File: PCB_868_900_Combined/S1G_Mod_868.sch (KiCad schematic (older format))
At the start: 56 parts, among them Q1 DMG2307L-7, SW1 CUS-12TB, T1 0732511150, U1 AP7361-33FGE-7, U2 ADF7023BCPZ, X1 ABS05-32.768KHZ-9-T, X2 ABM11-140-26.000MHZ-T3

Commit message: LDO and Pwr LEd
Power LED added to combined radio and LDO section revamped.
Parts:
- added LED4: LTST-C193KRKT-5A, PCB_Footprints:LED0603, symbol LTST-C193KRKT-5A
- added R10: RC1608J202CS, PCB_Footprints:R0603, symbol RC1608J202CS
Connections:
- wire segments 93 -> 95
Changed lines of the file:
@@
 $EndComp
 $Comp
-L GND #PWR24
+L GND #PWR26
 U 1 1 58161058
 P 7275 6075
-F 0 "#PWR24" H 7275 5825 50  0001 C CNN
+F 0 "#PWR26" H 7275 5825 50  0001 C CNN
 F 1 "GND" H 7280 5902 50  0000 C CNN
 F 2 "" H 7275 6075 50  0000 C CNN
@@
 $EndComp
 $Comp
-L GND #PWR19
+L GND #PWR21
 U 1 1 5816222C
 P 6125 4325
-F 0 "#PWR19" H 6125 4075 50  0001 C CNN
+F 0 "#PWR21" H 6125 4075 50  0001 C CNN
 F 1 "GND" H 6130 4152 50  0000 C CNN
 F 2 "" H 6125 4325 50  0000 C CNN
@@
 $EndComp
 $Comp
-L +3.3V #PWR17
+L +3.3V #PWR19
 U 1 1 581623E1
 P 5675 2075
-F 0 "#PWR17" H 5675 1925 50  0001 C CNN
+F 0 "#PWR19" H 5675 1925 50  0001 C CNN
 F 1 "+3.3V" H 5690 2248 50  0000 C CNN
 F 2 "" H 5675 2075 50  0000 C CNN
@@
 $EndComp
 $Comp
-L GND #PWR14
+L GND #PWR16
 U 1 1 58162F98
 P 5225 3250
-F 0 "#PWR14" H 5225 3000 50  0001 C CNN
+F 0 "#PWR16" H 5225 3000 50  0001 C CNN
 F 1 "GND" H 5230 3077 50  0000 C CNN
 F 2 "" H 5225 3250 50  0000 C CNN
@@
 $EndComp
 $Comp
-L GND #PWR22
+L GND #PWR24
 U 1 1 58164E94
 P 6475 5000
-F 0 "#PWR22" H 6475 4750 50  0001 C CNN
+F 0 "#PWR24" H 6475 4750 50  0001 C CNN
 F 1 "GND" H 6480 4827 50  0000 C CNN
 F 2 "" H 6475 5000 50  0000 C CNN
@@
 $EndComp
 $Comp
-L GND #PWR25
+L GND #PWR27
 U 1 1 58165059
 P 7525 5000
-F 0 "#PWR25" H 7525 4750 50  0001 C CNN
+F 0 "#PWR27" H 7525 4750 50  0001 C CNN
 F 1 "GND" H 7530 4827 50  0000 C CNN
 F 2 "" H 7525 5000 50  0000 C CNN
@@
 $EndComp
 $Comp
-L GND #PWR23
+L GND #PWR25
 U 1 1 58165567
 P 7125 5000
-F 0 "#PWR23" H 7125 4750 50  0001 C CNN
+F 0 "#PWR25" H 7125 4750 50  0001 C CNN
 F 1 "GND" H 7130 4827 50  0000 C CNN
 F 2 "" H 7125 5000 50  0000 C CNN
@@
 $EndComp
 $Comp
-L GND #PWR29
+L GND #PWR31
 U 1 1 58168376
 P 8850 5425
-F 0 "#PWR29" H 8850 5175 50  0001 C CNN
+F 0 "#PWR31" H 8850 5175 50  0001 C CNN
 F 1 "GND" H 8855 5252 50  0000 C CNN
 F 2 "" H 8850 5425 50  0000 C CNN
@@
 $EndComp
 $Comp
-L +3.3V #PWR20
+L +3.3V #PWR22
 U 1 1 58168986
 P 6150 1275
-F 0 "#PWR20" H 6150 1125 50  0001 C CNN
+F 0 "#PWR22" H 6150 1125 50  0001 C CNN
 F 1 "+3.3V" H 6165 1448 50  0000 C CNN
 F 2 "" H 6150 1275 50  0000 C CNN
@@
 $EndComp
 $Comp
-L GND #PWR13
+L GND #PWR15
 U 1 1 58169314
 P 5225 2300
-F 0 "#PWR13" H 5225 2050 50  0001 C CNN
+F 0 "#PWR15" H 5225 2050 50  0001 C CNN
 F 1 "GND" H 5230 2127 50  0000 C CNN
 F 2 "" H 5225 2300 50  0000 C CNN
@@
 $EndComp
 $Comp
-L GND #PWR9
+L GND #PWR10
 U 1 1 5816BC64
 P 3700 6900
-F 0 "#PWR9" H 3700 6650 50  0001 C CNN
+F 0 "#PWR10" H 3700 6650 50  0001 C CNN
 F 1 "GND" H 3705 6727 50  0000 C CNN
 F 2 "" H 3700 6900 50  0000 C CNN
@@
 $EndComp
 $Comp
-L GND #PWR16
+L GND #PWR18
 U 1 1 5816BFC1
 P 5575 6900
-F 0 "#PWR16" H 5575 6650 50  0001 C CNN
+F 0 "#PWR18" H 5575 6650 50  0001 C CNN
 F 1 "GND" H 5580 6727 50  0000 C CNN
 F 2 "" H 5575 6900 50  0000 C CNN
@@
 $EndComp
 $Comp
-L +3.3V #PWR15
+L +3.3V #PWR17
 U 1 1 5816C55D
 P 5575 6450
-F 0 "#PWR15" H 5575 6300 50  0001 C CNN
+F 0 "#PWR17" H 5575 6300 50  0001 C CNN
 F 1 "+3.3V" H 5590 6623 50  0000 C CNN
 F 2 "" H 5575 6450 50  0000 C CNN
@@
 MCU_IRQ
 $Comp
-L GND #PWR21
+L GND #PWR23
 U 1 1 58175F58
 P 6450 1775
-F 0 "#PWR21" H 6450 1525 50  0001 C CNN
+F 0 "#PWR23" H 6450 1525 50  0001 C CNN
 F 1 "GND" H 6455 1602 50  0000 C CNN
 F 2 "" H 6450 1775 50  0000 C CNN
@@
 $EndComp
 $Comp
-L GND #PWR26
+L GND #PWR28
 U 1 1 581763CA
 P 7950 1775
-F 0 "#PWR26" H 7950 1525 50  0001 C CNN
+F 0 "#PWR28" H 7950 1525 50  0001 C CNN
 F 1 "GND" H 7955 1602 50  0000 C CNN
 F 2 "" H 7950 1775 50  0000 C CNN
@@
 $EndComp
 $Comp
-L GND #PWR10
+L GND #PWR11
 U 1 1 5817CEBD
 P 3925 2150
-F 0 "#PWR10" H 3925 1900 50  0001 C CNN
+F 0 "#PWR11" H 3925 1900 50  0001 C CNN
 F 1 "GND" H 3930 1977 50  0000 C CNN
 F 2 "" H 3925 2150 50  0000 C CNN
@@
 $EndComp
 $Comp
-L GND #PWR12
+L GND #PWR13
 U 1 1 5817CF2D
 P 4725 2150
-F 0 "#PWR12" H 4725 1900 50  0001 C CNN
+F 0 "#PWR13" H 4725 1900 50  0001 C CNN
 F 1 "GND" H 4730 1977 50  0000 C CNN
 F 2 "" H 4725 2150 50  0000 C CNN
@@
 $EndComp
 $Comp
-L GND #PWR11
+L GND #PWR12
 U 1 1 58195E9E
 P 4525 4050
-F 0 "#PWR11" H 4525 3800 50  0001 C CNN
+F 0 "#PWR12" H 4525 3800 50  0001 C CNN
 F 1 "GND" H 4530 3877 50  0000 C CNN
 F 2 "" H 4525 4050 50  0000 C CNN
@@
 $EndComp
 $Comp
-L GND #PWR8
+L GND #PWR9
 U 1 1 58196935
 P 3650 2975
-F 0 "#PWR8" H 3650 2725 50  0001 C CNN
+F 0 "#PWR9" H 3650 2725 50  0001 C CNN
 F 1 "GND" H 3655 2802 50  0000 C CNN
 F 2 "" H 3650 2975 50  0000 C CNN
@@
 $EndComp
 $Comp
-L +3.3V #PWR28
+L +3.3V #PWR30
 U 1 1 581AA58C
 P 8625 2550
-F 0 "#PWR28" H 8625 2400 50  0001 C CNN
+F 0 "#PWR30" H 8625 2400 50  0001 C CNN
 F 1 "+3.3V" H 8640 2723 50  0000 C CNN
 F 2 "" H 8625 2550 50  0000 C CNN
@@
 NoConn ~ 10350 6050
 $Comp
-L GND #PWR18
+L GND #PWR20
 U 1 1 5822EA21
 P 5750 7525
-F 0 "#PWR18" H 5750 7275 50  0001 C CNN
+F 0 "#PWR20" H 5750 7275 50  0001 C CNN
 F 1 "GND" H 5755 7352 50  0000 C CNN
 F 2 "" H 5750 7525 50  0000 C CNN
@@
 	7375 2025 7375 2500
 $Comp
-L GND #PWR27
+L GND #PWR29
 U 1 1 582AA168
 P 8100 2475
-F 0 "#PWR27" H 8100 2225 50  0001 C CNN
+F 0 "#PWR29" H 8100 2225 50  0001 C CNN
 F 1 "GND" H 8105 2302 50  0000 C CNN
 F 2 "" H 8100 2475 50  0000 C CNN
@@
 NoConn ~ 9125 5075
 NoConn ~ 9125 5550
+$Comp
+L LTST-C193KRKT-5A LED4
+U 1 1 582B8889
+P 4950 5850
+F 0 "LED4" H 4950 6097 60  0000 C CNN
+F 1 "LTST-C193KRKT-5A" H 4950 5991 60  0000 C CNN
+F 2 "PCB_Footprints:LED0603" H 6375 7775 60  0001 C CNN
+F 3 "http://optoelectronics.liteon.com/upload/download/DS22-2005-077/S_110_LTST-C193KRKT-5A.pdf" H 6575 7900 60  0001 C CNN
+F 4 "0.07565 @ 1000" H 4800 6050 60  0001 C CNN "Cost"
+F 5 "11 Nov 2016" H 4900 6150 60  0001 C CNN "Date Created"
+F 6 "11 Nov 2016" H 5000 6250 60  0001 C CNN "Date Modified"
+F 7 "Adam Vadala-Roth" H 5100 6350 60  0001 C CNN "Designer"
+F 8 "0.55mm" H 5200 6450 60  0001 C CNN "Height"
+F 9 "Yes" H 5300 6550 60  0001 C CNN "RhoS?"
+F 10 "Lite-On Inc" H 5400 6650 60  0001 C CNN "MFR"
+F 11 "LTST-C193KRKT-5A" H 5500 6750 60  0001 C CNN "MFR#"
+F 12 "SMT/SMD" H 5600 6850 60  0001 C CNN "Mounting"
+F 13 "2" H 5700 6950 60  0001 C CNN "Pin Count#"
+F 14 "Active" H 5800 7050 60  0001 C CNN "Status"
+F 15 "N/A" H 5900 7150 60  0001 C CNN "Tolerance"
+F 16 "0603 LED" H 6000 7250 60  0001 C CNN "Type"
+F 17 "2.8V Forward Voltage" H 6100 7350 60  0001 C CNN "Voltage"
+F 18 "N/A" H 6200 7450 60  0001 C CNN "Wattage"
+F 19 "N/A" H 6300 7550 60  0001 C CNN "Component-Value"
+F 20 "Red 631nm LED Indication - Discrete 2V 0603 (1608 Metric)" H 6400 7650 60  0001 C CNN "Description"
+	1    4950 5850
+	1    0    0    -1
+$EndComp
+$Comp
+L RC1608J202CS R10
+U 1 1 582B8A24
+P 4125 5850
+F 0 "R10" H 4125 6203 60  0000 C CNN
+F 1 "RC1608J202CS" H 4125 6097 60  0000 C CNN
+F 2 "PCB_Footprints:R0603" H 3725 6100 60  0001 C CNN
+F 3 "https://media.digikey.com/pdf/Data%20Sheets/Samsung%20PDFs/RC_Series_ds.pdf" H 3825 6300 60  0001 C CNN
+F 4 "0.00268 @ 5000" H 5675 7800 60  0001 C CNN "Cost"
+F 5 "14 Sept 2016" H 4025 6400 60  0001 C CNN "Date Created"
+F 6 "14 Sept 2016" H 4125 6500 60  0001 C CNN "Date Modified"
+F 7 "Adam Vadala-Roth" H 4225 6600 60  0001 C CNN "Designer"
+F 8 "0.55mm" H 4325 6700 60  0001 C CNN "Height"
+F 9 "Yes" H 4425 6800 60  0001 C CNN "RHoS?"
+F 10 "Samsung Electro-Mechanics America, Inc." H 4525 6900 60  0001 C CNN "MFR"
+F 11 "RC1608F202CS" H 4625 7000 60  0001 C CNN "MFR#"
+F 12 "SMT/SMD" H 4725 7100 60  0001 C CNN "Mounting"
+F 13 "2" H 4825 7200 60  0001 C CNN "Pin Count#"
+F 14 "Active" H 4925 7300 60  0001 C CNN "Status"
+F 15 "1%" H 5025 7400 60  0001 C CNN "Tolerance"
+F 16 "passive" H 5125 7500 60  0001 C CNN "Type"
+F 17 "N/A" H 5225 7600 60  0001 C CNN "Voltage"
+F 18 "1/10" H 5325 7700 60  0001 C CNN "Wattage"
+F 19 "2k" H 4125 5991 60  0000 C CNN "Component-Value"
+F 20 "RES SMD 2K OHM 1% 1/10W 0603" H 5525 7900 60  0001 C CNN "Description"
+	1    4125 5850
+	1    0    0    -1
+$EndComp
+$Comp
+L GND #PWR14
+U 1 1 582B9301
+P 5200 5850
+F 0 "#PWR14" H 5200 5600 50  0001 C CNN
+F 1 "GND" H 5205 5677 50  0000 C CNN
+F 2 "" H 5200 5850 50  0000 C CNN
+F 3 "" H 5200 5850 50  0000 C CNN
+	1    5200 5850
+	1    0    0    -1
+$EndComp
+Wire Wire Line
+	4700 5850 4425 5850
+$Comp
+L +3.3V #PWR8
+U 1 1 582B94B0
+P 3550 5850
+F 0 "#PWR8" H 3550 5700 50  0001 C CNN
+F 1 "+3.3V" H 3565 6023 50  0000 C CNN
+F 2 "" H 3550 5850 50  0000 C CNN
+F 3 "" H 3550 5850 50  0000 C CNN
+	1    3550 5850
+	1    0    0    -1
+$EndComp
+Wire Wire Line
+	3825 5850 3550 5850
 $EndSCHEMATC

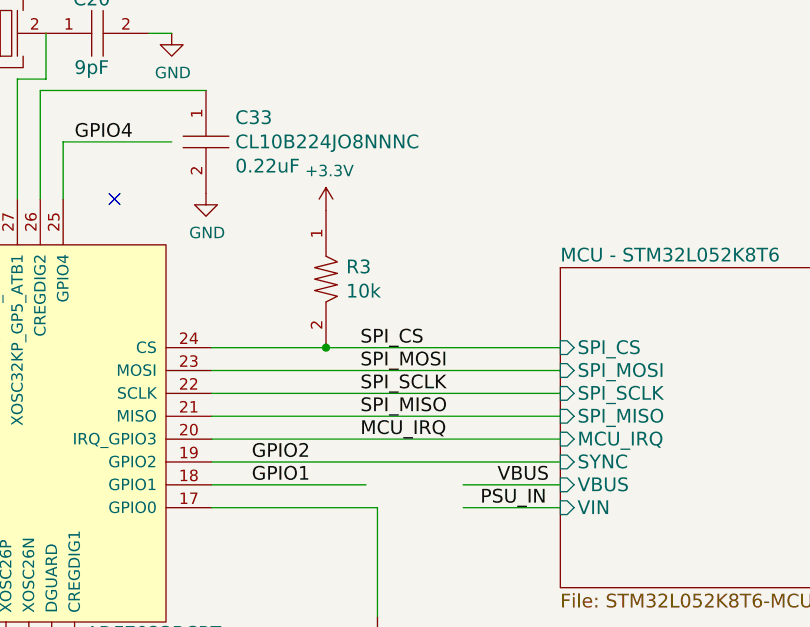
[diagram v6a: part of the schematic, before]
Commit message: SPI Resistors
SPI resistors added to combined antenna implementation.
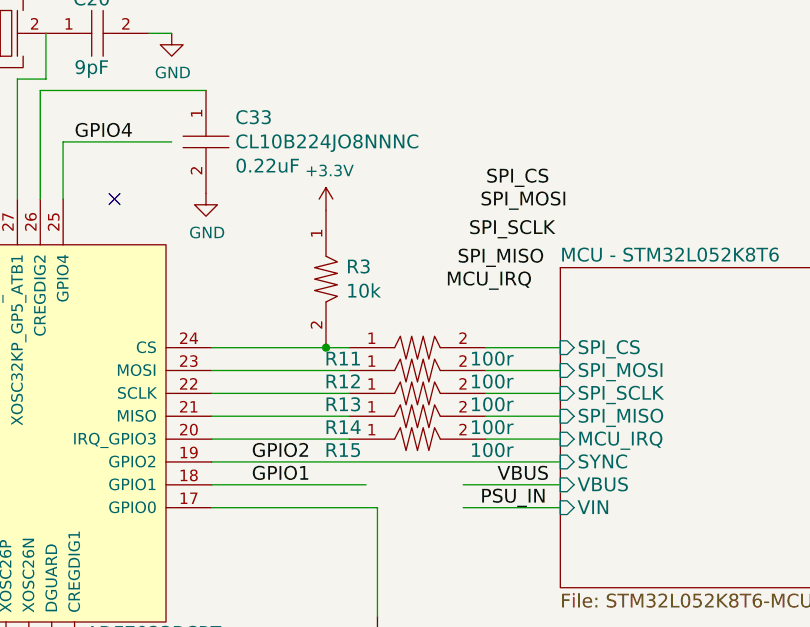
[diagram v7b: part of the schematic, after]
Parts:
- added R11, R12, R13, R14, R15: TNPW0402100RBEED, PCB_Footprints:R0402, symbol TNPW0402100RBEED
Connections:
- wire segments 95 -> 100

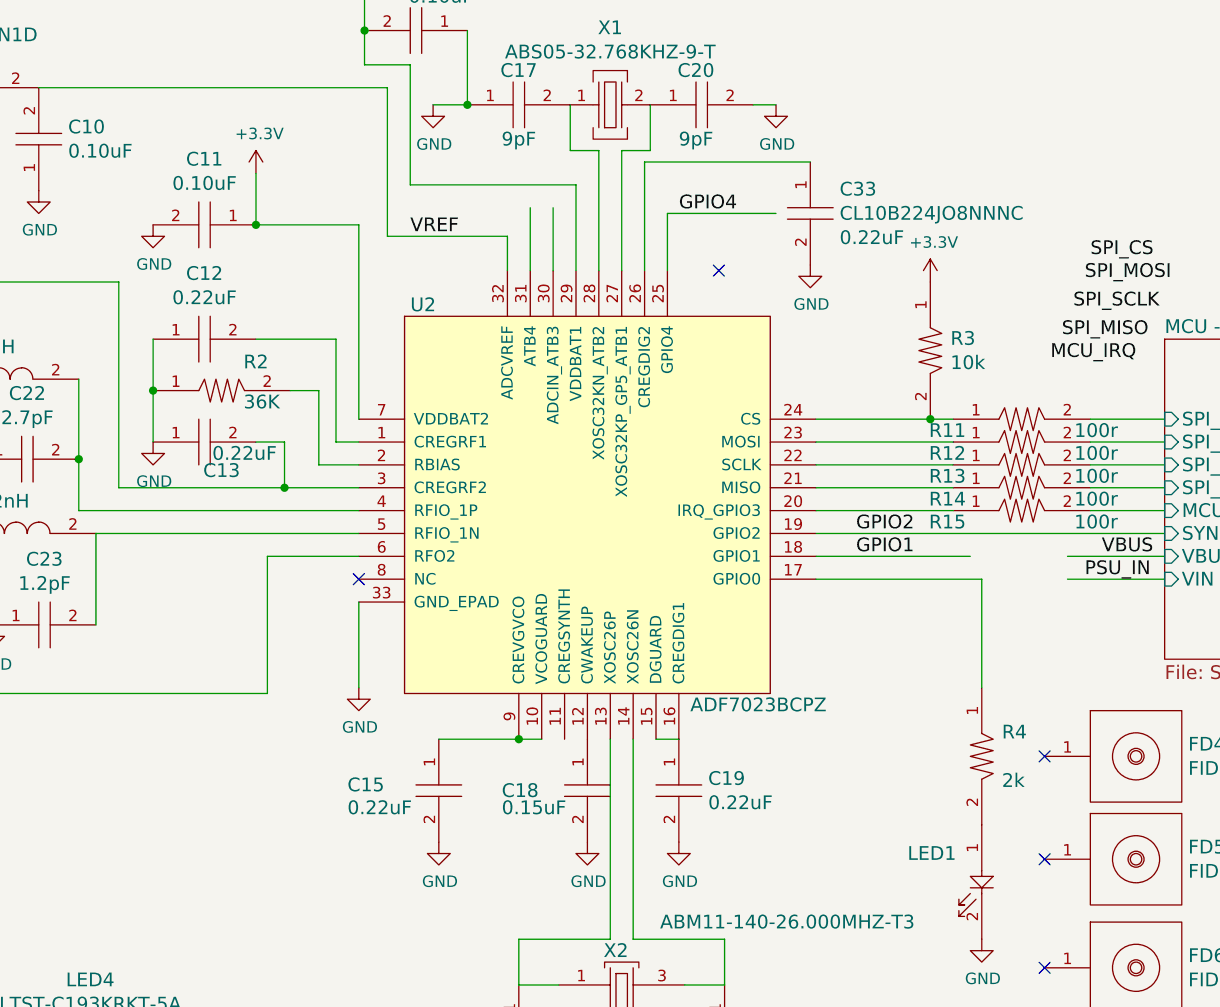
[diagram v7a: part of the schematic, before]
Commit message: 0.22uF cap
0.22uF cap replaced with 0402 part instead of the massive 0603 part.
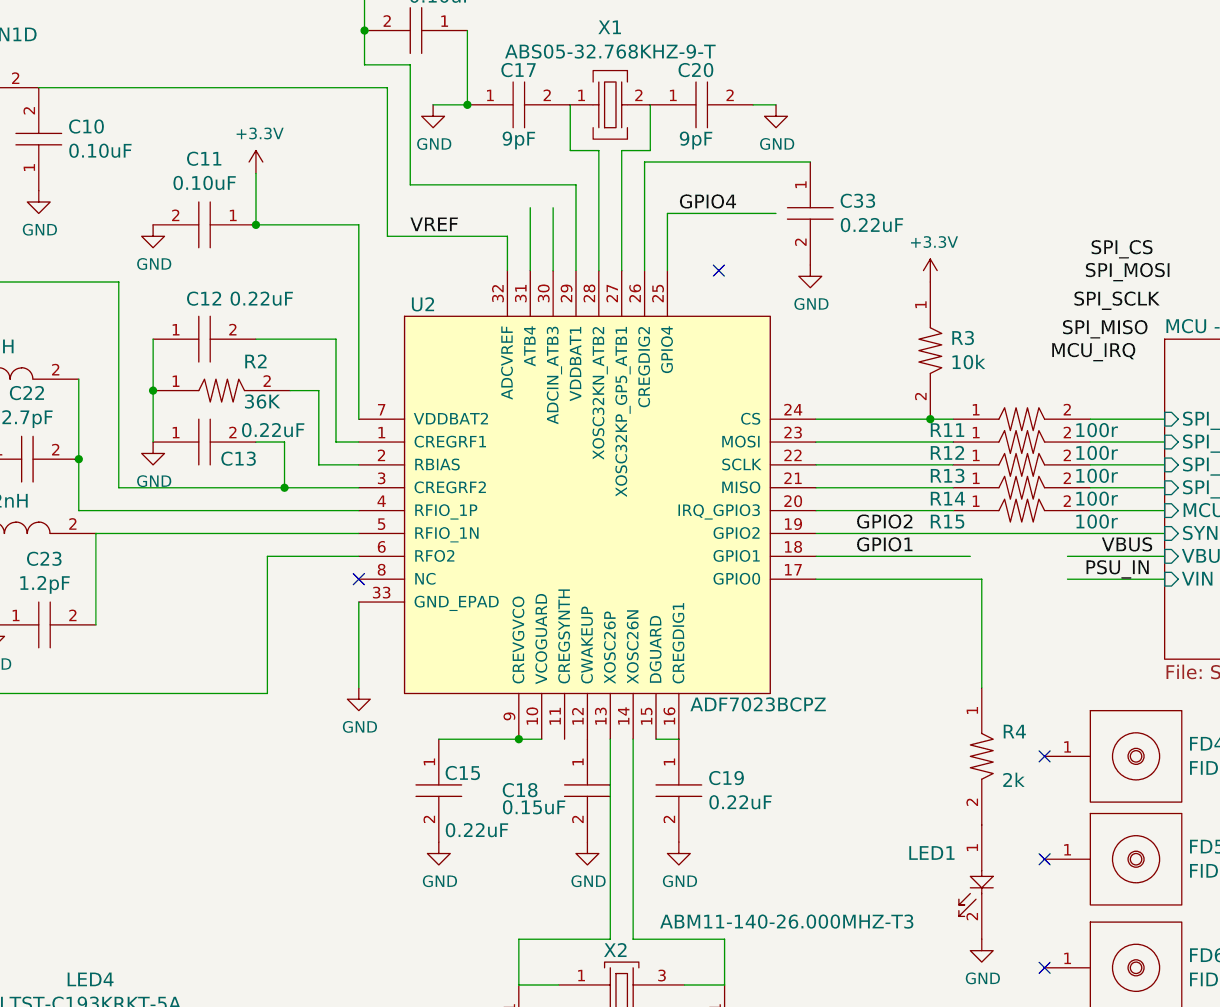
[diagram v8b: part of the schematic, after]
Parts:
- removed C12, C13, C15, C19, C33: CL10B224JO8NNNC, PCB_Footprints:C0402, symbol CL10B224JO8NNNC
- added C12, C13, C15, C19, C33: CL05A224KP5NNNC, PCB_Footprints:C0402, symbol CL05A224KP5NNNC
